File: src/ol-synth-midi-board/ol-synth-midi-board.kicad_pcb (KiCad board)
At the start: 2 copper layers, 101.6 x 69.8 mm, 10 parts, among them J1 MIDI_IO_HEADER, J2 MIDI_IN, J3 MIDI_OUT, U1 H11L1

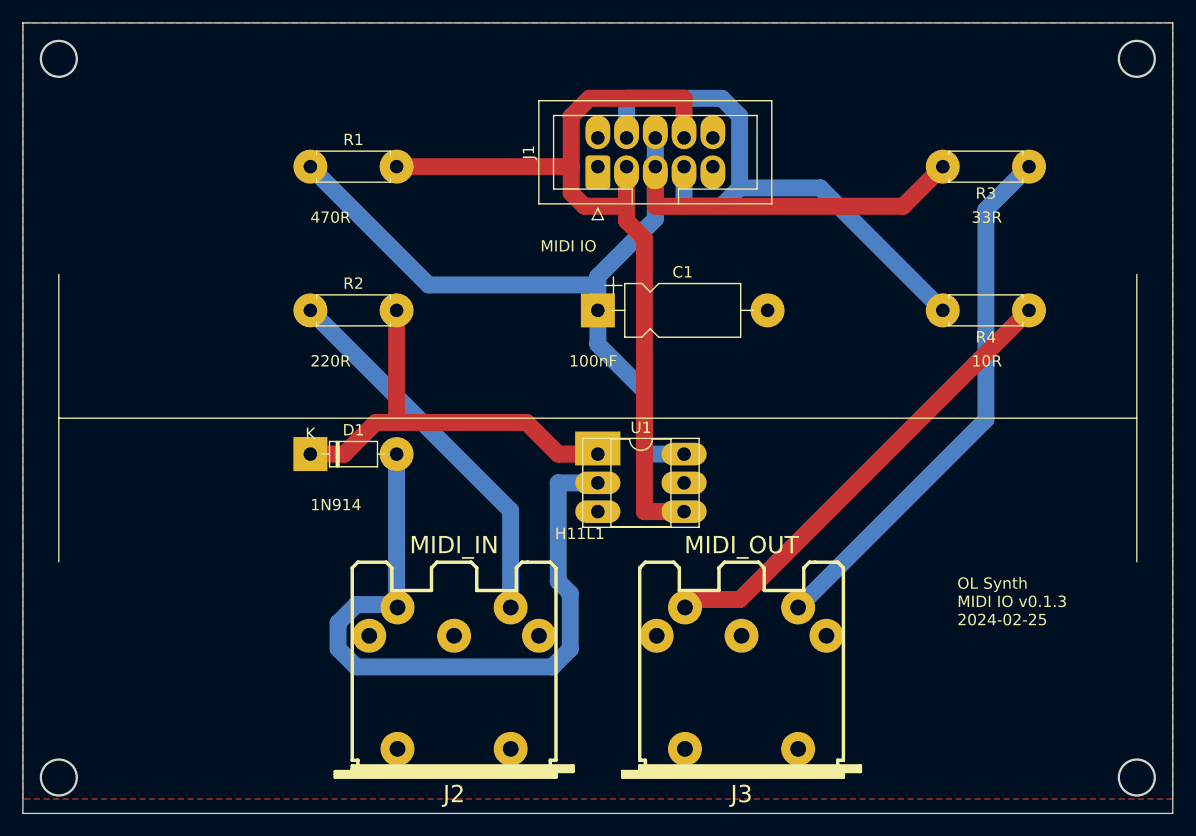
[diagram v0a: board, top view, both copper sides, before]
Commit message: - added fixture deep outline engraving gcode
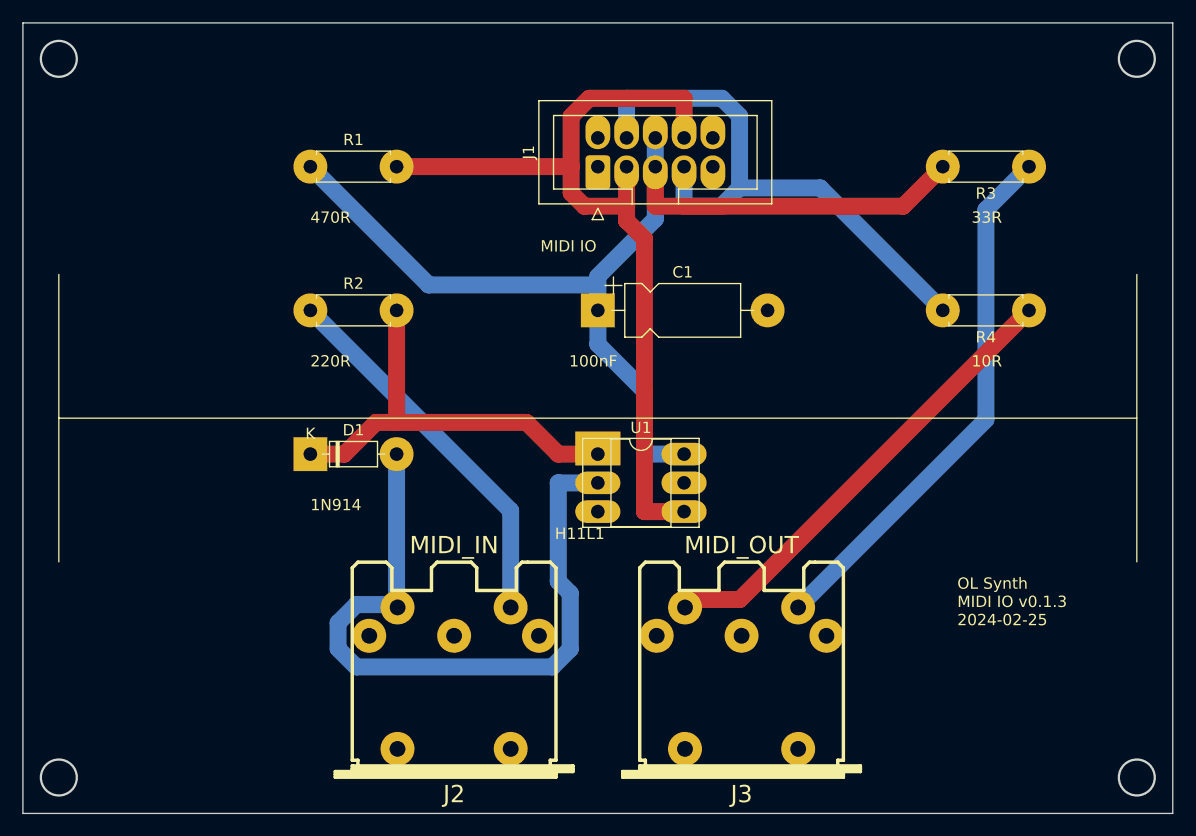
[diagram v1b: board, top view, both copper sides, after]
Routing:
- removed copper zone on F.Cu, net GND
